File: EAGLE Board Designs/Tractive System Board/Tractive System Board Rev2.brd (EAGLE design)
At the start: 206.7 x 150.3 mm, 179 parts, among them J3 CONNECTOR-8_MF_T_V_, J5 CONNECTOR-4__, K4 RELAY_SPST_NC_POLARIZED_D_12, K5 RELAY_SPST_NO_D_12, Q2 TRANSISTOR_N_MOS__PMV15ENEA, U1 LTC6994_1, U10 DCM4623TD2J13D0T70, U11 RELAY_SOLIDSTATE_NC_AG, U15 LOGICGATE_INVERTER_DCKR, U16 LTC3639, U17 VOLTAGE_REGULATOR_ADJ_LR8_DPAK, U18 ISO224B_AIRGAP, U19 ISO224B_AIRGAP, U2 VOLTAGE_REGULATOR_SOT223_5V

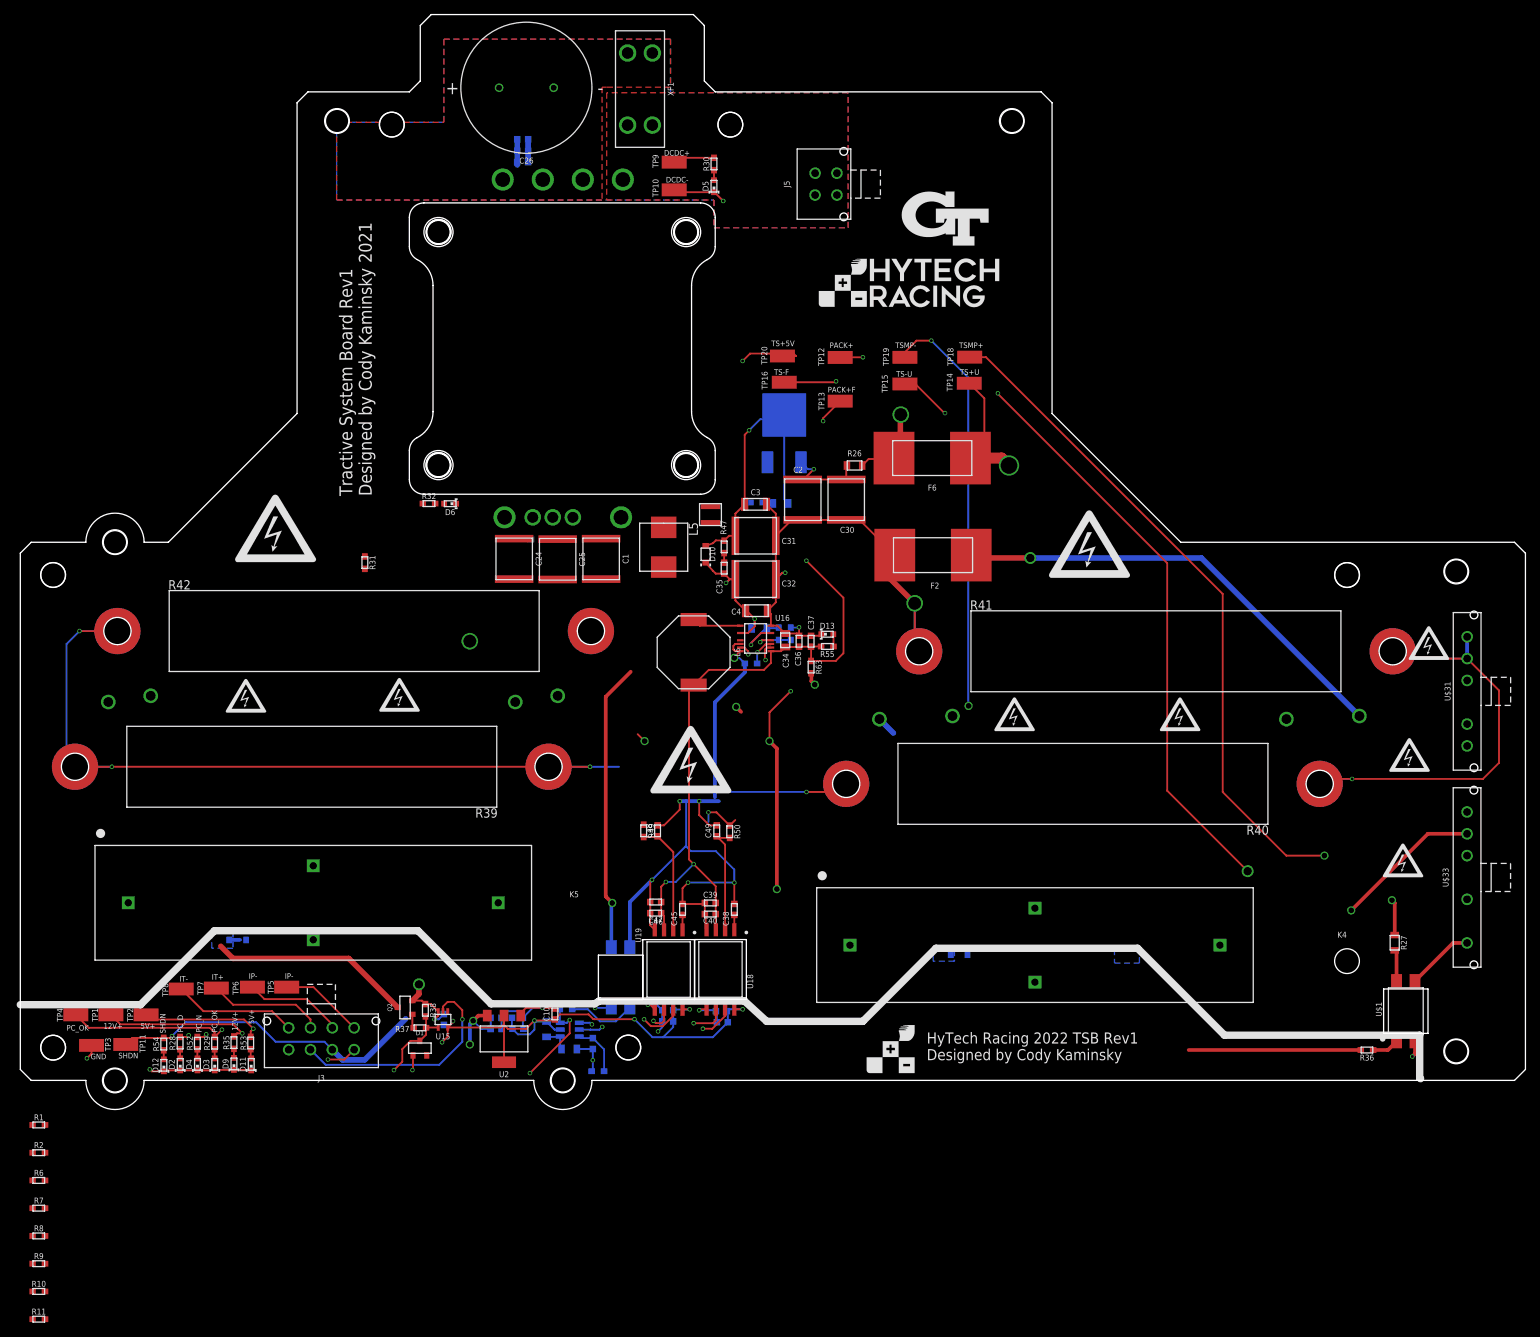
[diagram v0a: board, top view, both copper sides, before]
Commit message: Made the major schematic and board design changes needed for the last rev
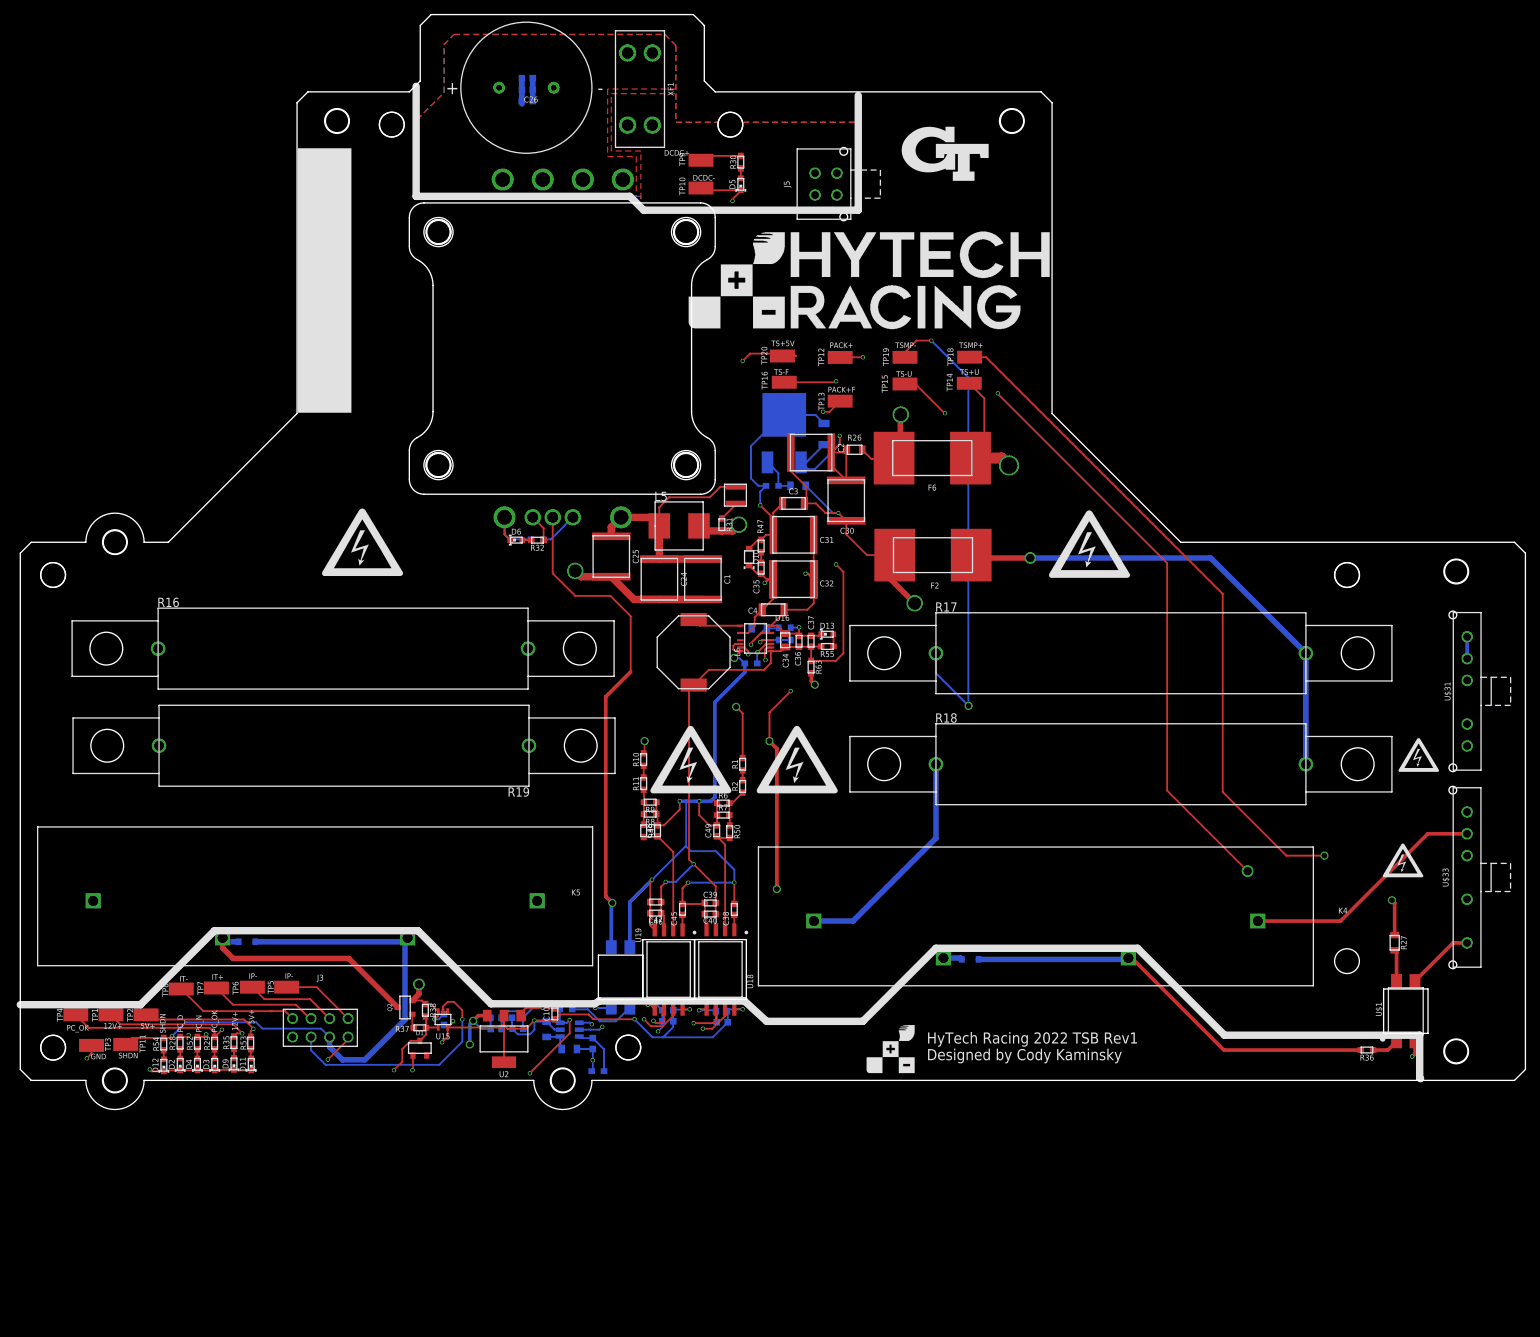
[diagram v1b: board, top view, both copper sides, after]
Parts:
- removed R39: RESISTOR_GND_750, HyTechDevicesTempTSB:B20
- removed R40, R41, R42: RESISTOR_GND_10K, HyTechDevicesTempTSB:B20
- removed U$49, U$50: (no value), HyTechAesthetics:HV_0.50"
- removed U$51: (no value), HyTechAesthetics:HV_1.00"
- removed U$53: (no value), HyTechAesthetics:LOGO_HYTECH_1.0"
- added D14: RECTIFIER_400V_SOD123, HyTechDevicesTempTSB:SOD123F
- added R16, R17, R18: RESISTOR_B20_10K, HyTechDevices:B20
- added R19: RESISTOR_B20_750, HyTechDevices:B20
- J3: value CONNECTOR-8_MF_T_V_ -> CONNECTOR-8__; device HyTechDevices:MOLEX_MICROFIT_PTH_VERTICAL_08_DUAL -> HyTechDevices:FLEX_STACK_PTH_08_DUAL
- K4: value RELAY_SPST_NC_POLARIZED_D_12 -> RELAY_SPST_NC_POLARIZED_3550_12; device HyTechDevices:D -> HyTechDevices:335X
- K5: value RELAY_SPST_NO_D_12 -> RELAY_SPST_NO_3550_12; device HyTechDevices:D -> HyTechDevices:335X
- R43: value RESISTOR_0805_365K -> RESISTOR_0805_HV365K
- U$43: device HyTechAesthetics:HV_0.50" -> HyTechManufacturing:LOGO_HYTECH_LARGE
- U$46, U$47: device HyTechAesthetics:HV_0.50" -> HyTechManufacturing:HV_LARGE
- moved R11 110.9 mm to (85.6, 39.2), turned to 90 degrees
- moved R10 110.6 mm to (85.6, 42.5), turned to 90 degrees
- moved U$43 110.5 mm to (91.7, 101.7)
- moved R2 108.9 mm to (99.2, 38.9), turned to 90 degrees
- moved R1 108.6 mm to (99.2, 41.9), turned to 90 degrees
- moved R7 108.4 mm to (96.5, 34.9)
- moved R6 107.3 mm to (96.5, 36.6)
- moved R9 105.2 mm to (86.5, 36.7), turned to 180 degrees
- moved R8 102.0 mm to (86.5, 35.1), turned to 180 degrees
- moved U$46 92.6 mm to (47.0, 72.4)
- moved U$47 52.9 mm to (106.7, 42.5)
- moved R31 49.3 mm to (96.3, 74.8)
- moved C24 20.1 mm to (87.8, 67.3)
- moved R32 15.7 mm to (71.0, 72.7), turned to 180 degrees
- moved C1 14.2 mm to (93.7, 67.3)
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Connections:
- net N$15: now also D14.C
- net N$50: now also K5.4, R19.1; no longer K5.1, R39.1
- net N$51: now also K4.4, R18.2; no longer K4.1, R40.1
- net N$58: now also D14.A
- net PACK+: now also K5.1; no longer K5.2
- net SHDN: now also K4.2, K5.2; no longer K4.4, K5.4
- net TS+UNFUSED: now also K4.1, R16.1, R19.2; no longer K4.2, R39.2, R42.1
- net TS-FUSED: no longer R39.3, R39.4, R39.5, R39.6, R40.3, R40.4, R40.5, R40.6, R41.3, R41.4, R41.5, R41.6, R42.3, R42.4, R42.5, R42.6
- net TS-UNFUSED: now also R17.1, R18.1; no longer R40.2, R41.1
- net TSMP+: now also R16.2; no longer R42.2
- net TSMP-: now also R17.2; no longer R41.2
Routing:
- net TS-FUSED: track 553.1 -> 413.6 mm, vias 15 -> 12
- net SHDN: track 173.3 -> 253.4 mm
- net N$39: track 2.37 -> 33.6 mm
- net N$51: track 2.71 -> 31.6 mm
- net ENABLE: track 39.7 -> 68.1 mm
- net N$50: track 0.00 -> 25.1 mm
- net N$15: track 12.4 -> 26.6 mm
- net TS+UNFUSED: track 253.0 -> 261.3 mm, vias 2 -> 1
- net TSMP+: track 287.7 -> 295.6 mm
- net N$8: track 0.00 -> 5.51 mm
- net PACK+: track 246.0 -> 251.5 mm
- net TS+FUSED: track 253.1 -> 258.5 mm
- net N$45: track 0.00 -> 5.30 mm
- net N$13: track 0.01 -> 4.82 mm
- net TSMP-: track 131.7 -> 136.0 mm
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- removed copper zone on layer 16, net GND
- removed copper zone on layer 16, net N$40
- removed copper zone on layer 16, net SHDN
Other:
- board text removed: "Tractive System Board Rev1 Designed by Cody Kaminsky 2021"

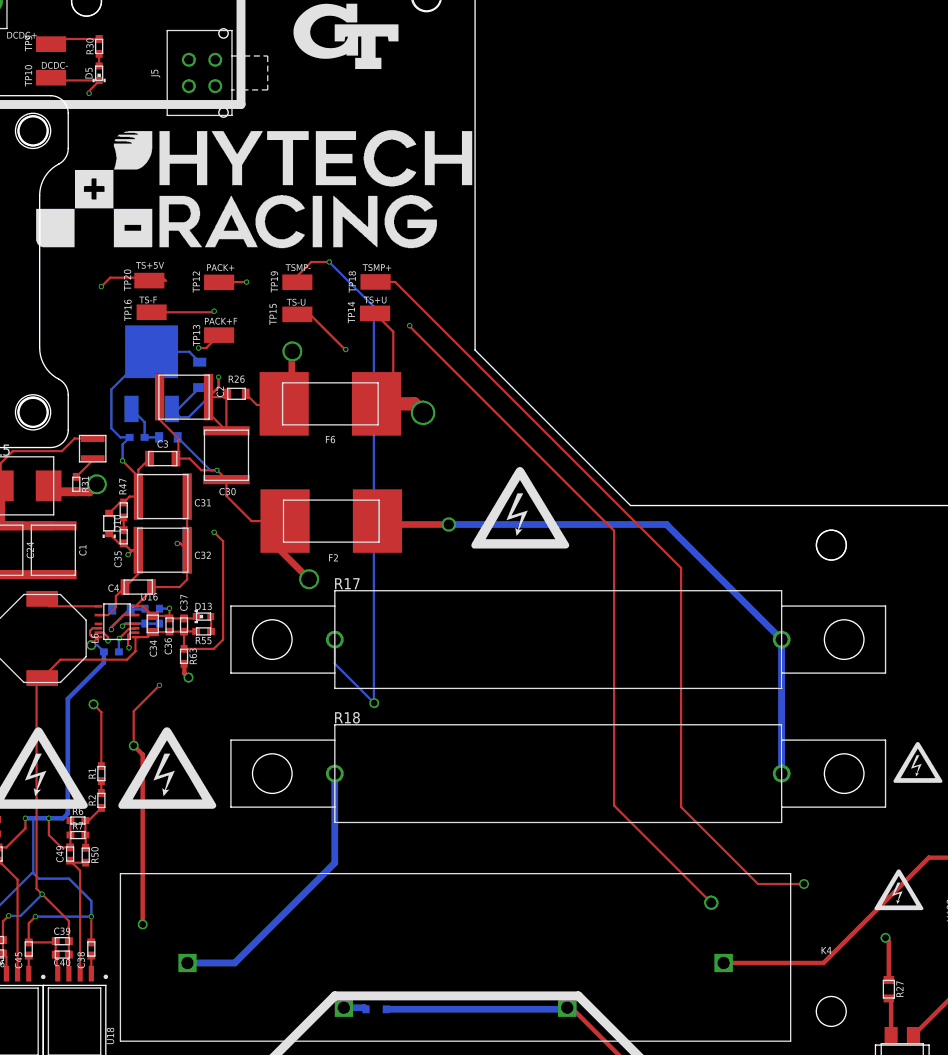
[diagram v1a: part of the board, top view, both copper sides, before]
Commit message: Made final changes to schematic
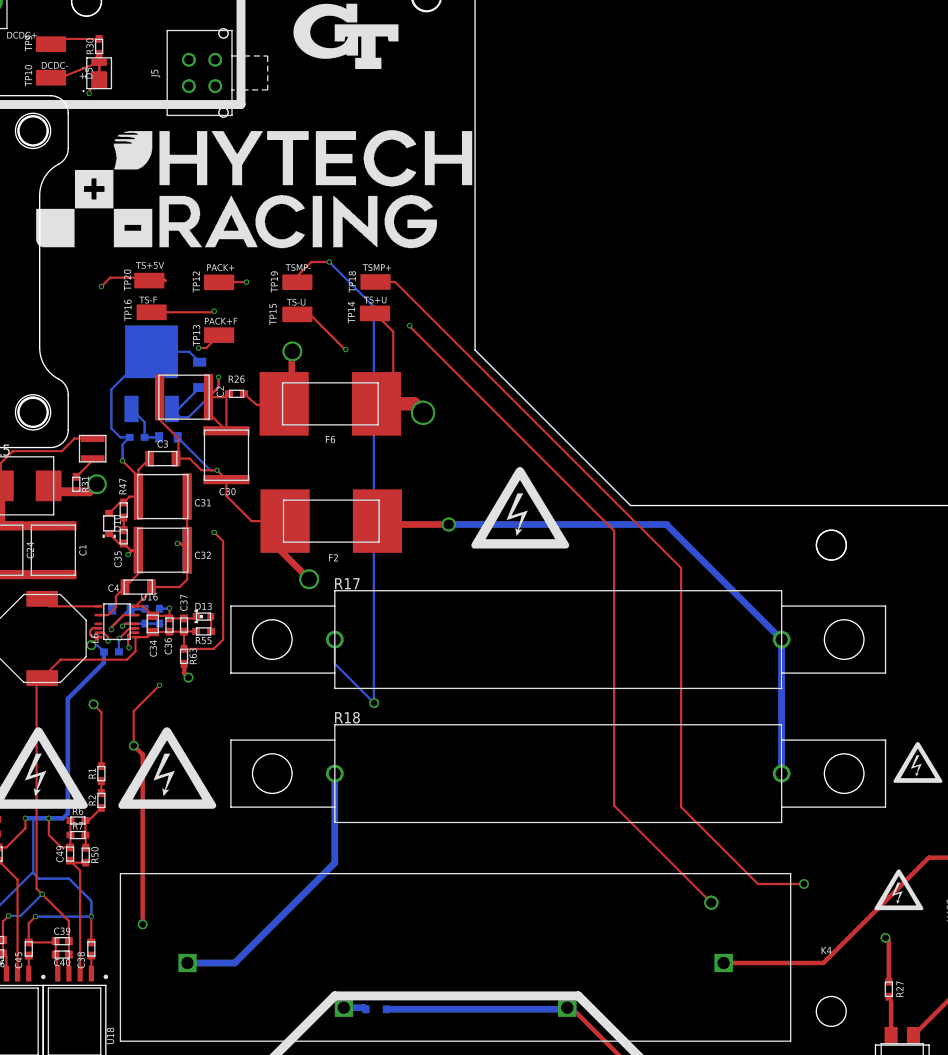
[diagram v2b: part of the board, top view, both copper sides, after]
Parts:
- D12: value LED_0603_WHITE -> LED_0603_ORANGE
- D2: value LED_0603_ORANGE -> LED_0603_WHITE
- D3: value LED_0603_YELLOW -> LED_0603_GREEN
- D5: value LED_0603_WHITE -> LED_2835_BLUE; device HyTechDevices:0603-LED -> HyTechDevices:2835-LED
- R26: value RESISTOR_0805_1 -> RESISTOR_0603_3.3; device HyTechDevices:0805-RES -> HyTechDevices:0603-RES
- R27: value RESISTOR_0805_12.4 -> RESISTOR_0603_3.3; device HyTechDevices:0805-RES -> HyTechDevices:0603-RES
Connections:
- net DCDC-: now also D5.C; no longer D5.1
- net N$18: now also D5.A; no longer D5.2
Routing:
- net DCDC-: track 10.8 -> 13.2 mm
- net N$18: track 1.37 -> 2.93 mm

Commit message: Final changes to both
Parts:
- added U$53, U$70, U$71, U$75: (no value), HyTechManufacturing:TS
- added U$72, U$73, U$74: (no value), HyTechManufacturing:GLV
- D5: value LED_2835_BLUE -> LED_0603_BLUE; device HyTechDevices:2835-LED -> HyTechDevices:0603-LED
- U$56, U$57, U$58, U$59, U$60, U$61, U$62: device HyTechAesthetics:GLV -> HyTechManufacturing:GLV
- U$63, U$64, U$65, U$66, U$67, U$68, U$69: device HyTechAesthetics:TS -> HyTechManufacturing:TS
- moved U$62 176.1 mm to (2.41, 7.11)
- moved U$63 162.3 mm to (2.29, 10.4)
- moved U$69 161.5 mm to (164.1, 9.65)
- moved U$64 158.3 mm to (20.2, 16.0)
- moved U$61 132.0 mm to (26.2, 13.8)
- moved U$56 105.2 mm to (107.7, 4.83)
- moved U$57 99.9 mm to (122.2, 8.64)
- moved U$68 99.7 mm to (115.4, 9.78)
- moved U$58 97.3 mm to (155.7, 9.53)
- moved U$59 67.9 mm to (176.7, 2.79)
- moved U$60 66.5 mm to (55.5, 14.0)
- moved U$65 55.0 mm to (61.5, 15.9)
- moved U$67 6.48 mm to (71.8, 11.3)
- moved U$66 1.25 mm to (107.6, 8.51)
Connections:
- net DCDC-: now also D5.1; no longer D5.C
- net N$18: now also D5.2; no longer D5.A
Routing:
- net DCDC-: track 13.2 -> 10.8 mm
- net N$18: track 2.93 -> 1.37 mm
